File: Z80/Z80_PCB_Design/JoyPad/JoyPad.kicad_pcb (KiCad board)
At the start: 2 copper layers, 19 parts, among them J1 Conn_01x12, SW1 SW_Push, SW2 SW_Push, SW3 SW_Push, SW4 SW_Push, SW5 SW_Push, SW6 SW_Push, SW7 SW_Push, SW8 SW_Push

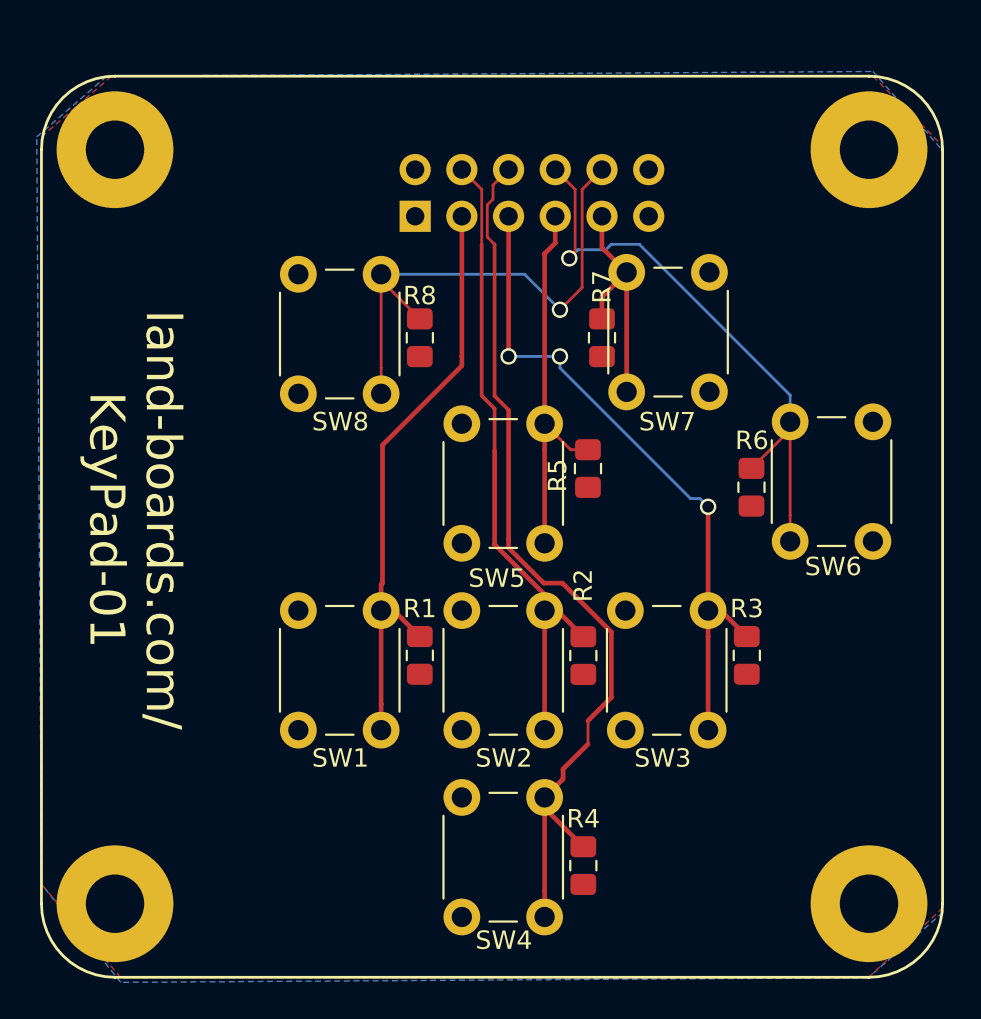
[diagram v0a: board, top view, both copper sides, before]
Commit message: Front panel toggle on LED release
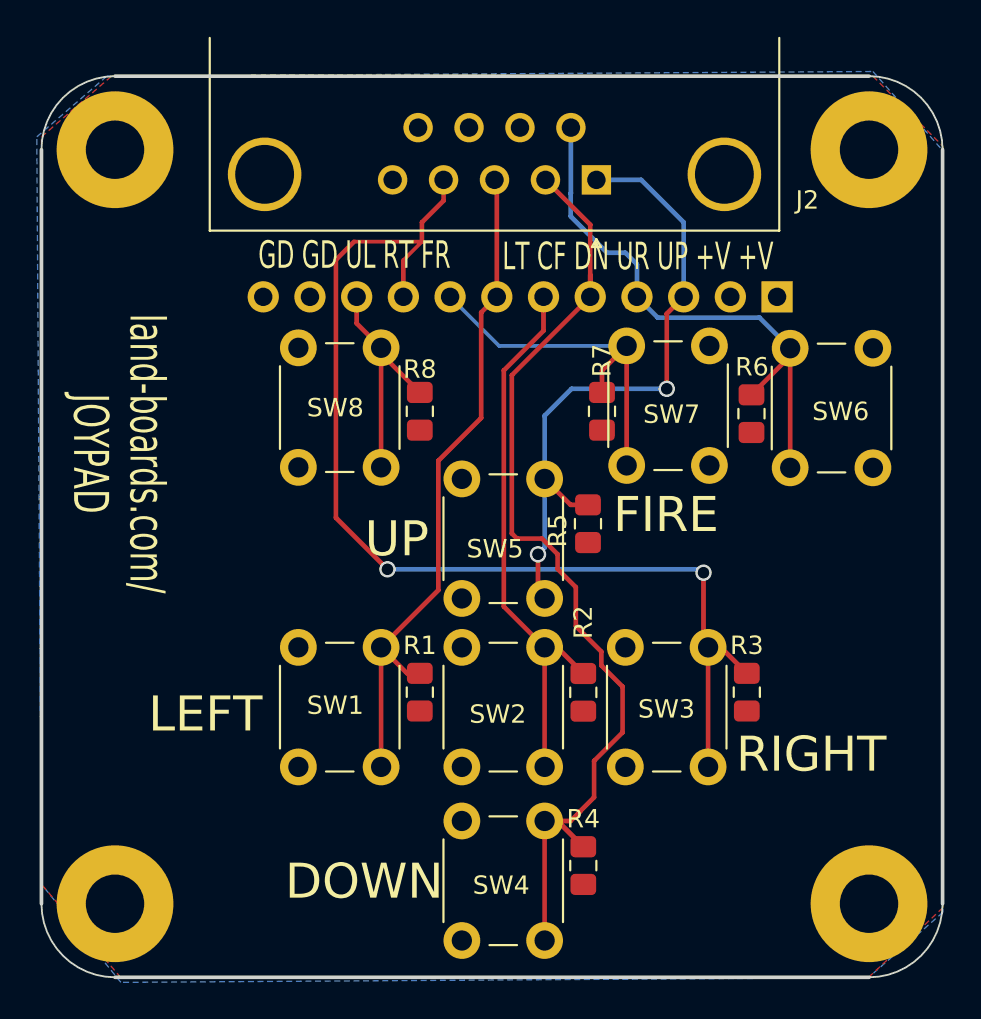
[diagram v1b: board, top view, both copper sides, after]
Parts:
- removed BD-49X49: VAL**, LandBoards_BoardOutlines:BD-49X49
- added J2: M09H, Connector_Dsub:DSUB-9_Male_Horizontal_P2.77x2.84mm_EdgePinOffset4.94mm_Housed_MountingHolesOffset7.48mm, F.Cu at (30.2, 5.64)
- added MTG1: MTG_HOLE, LandBoards_MountHoles:MTG-4-40, F.Cu at (4.00, 4.00)
- added MTG2: MTG_HOLE, LandBoards_MountHoles:MTG-4-40, F.Cu at (45.0, 4.00)
- added MTG3: MTG_HOLE, LandBoards_MountHoles:MTG-4-40, F.Cu at (4.00, 45.0)
- added MTG4: MTG_HOLE, LandBoards_MountHoles:MTG-4-40, F.Cu at (45.0, 45.0)
- J1: footprint Connector_PinSocket_2.54mm:PinSocket_2x06_P2.54mm_Horizontal -> Connector_PinHeader_2.54mm:PinHeader_1x12_P2.54mm_Vertical
- R1, R2, R3, R4, R5, R6, R7, R8: value 1K -> 10K
- moved J1 20.2 mm to (40.0, 12.0), turned to 90 degrees
- moved TEST 13.8 mm to (44.0, 33.0)
- moved R6 4.00 mm to (38.6, 18.4)
- moved R7 4.00 mm to (30.5, 18.2)
- moved R8 4.00 mm to (20.6, 18.2)
- moved SW6 4.00 mm to (45.2, 14.8)
- moved SW7 4.00 mm to (36.3, 14.7)
- moved SW8 4.00 mm to (14.0, 21.3)
- moved R5 3.00 mm to (29.7, 24.3)
- moved SW5 3.00 mm to (22.9, 28.4)
- moved R1 2.00 mm to (20.6, 33.5)
- moved R2 2.00 mm to (29.5, 33.5)
- moved R3 2.00 mm to (38.4, 33.5)
- moved SW1 2.00 mm to (14.0, 37.6)
- moved SW2 2.00 mm to (22.9, 37.6)
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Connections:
- net /S1D0 renamed /UL
- J1 pad 3: /S1D7 -> /UP
- J1 pad 4: /S1D6 -> /UR
- J1 pad 5: /S1D5 -> /DN
- J1 pad 6: /S1D4 -> /CF
- J1 pad 7: /S1D3 -> /LT
- J1 pad 8: /S1D2 -> /FR
- J1 pad 9: /S1D1 -> /RT
- R1 pad 2: /S1D7 -> /LT
- R2 pad 2: /S1D6 -> /CF
- R3 pad 2: /S1D5 -> /RT
- R4 pad 2: /S1D4 -> /DN
- R5 pad 2: /S1D3 -> /UP
- R6 pad 2: /S1D2 -> /UR
- R7 pad 2: /S1D1 -> /FR
- SW1 pad 2: /S1D7 -> /LT
- SW2 pad 2: /S1D6 -> /CF
- SW3 pad 2: /S1D5 -> /RT
- SW4 pad 2: /S1D4 -> /DN
- SW5 pad 2: /S1D3 -> /UP
- SW6 pad 2: /S1D2 -> /UR
- SW7 pad 2: /S1D1 -> /FR
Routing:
- net /RT: track 0.00 -> 61.0 mm, vias 0 -> 2
- net /DN: track 0.00 -> 56.9 mm
- net /S1D4: track 49.6 -> 0.00 mm
- net /S1D6: track 41.5 -> 0.00 mm
- net /LT: track 0.00 -> 37.3 mm
- net /S1D5: track 37.1 -> 0.00 mm, vias 3 -> 0
- net /UP: track 0.00 -> 35.6 mm, vias 0 -> 2
- net /S1D2: track 32.5 -> 0.00 mm, vias 1 -> 0
- net /S1D7: track 32.4 -> 0.00 mm
- net /UR: track 0.00 -> 31.5 mm
- net /CF: track 0.00 -> 30.9 mm
- net /S1D3: track 21.0 -> 0.00 mm
- net /FR: track 0.00 -> 20.3 mm
- net /UL: track 28.9 -> 13.1 mm, vias 1 -> 0
- net /S1D1: track 13.2 -> 0.00 mm
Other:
- board outline added: 49 x 49 mm
- board text added: "DOWN"
- board text added: "FIRE"
- board text added: "GD GD UL RT FR"
- board text added: "LEFT"
- board text added: "LT CF DN UR UP +V +V"
- board text added: "RIGHT"
- board text added: "UP"
- board text added: "land-boards.com/ JOYPAD"
- board text removed: "land-boards.com/ KeyPad-01"
